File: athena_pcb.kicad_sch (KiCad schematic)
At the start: 8 parts, among them U1 NRF5340-QKAA-R7

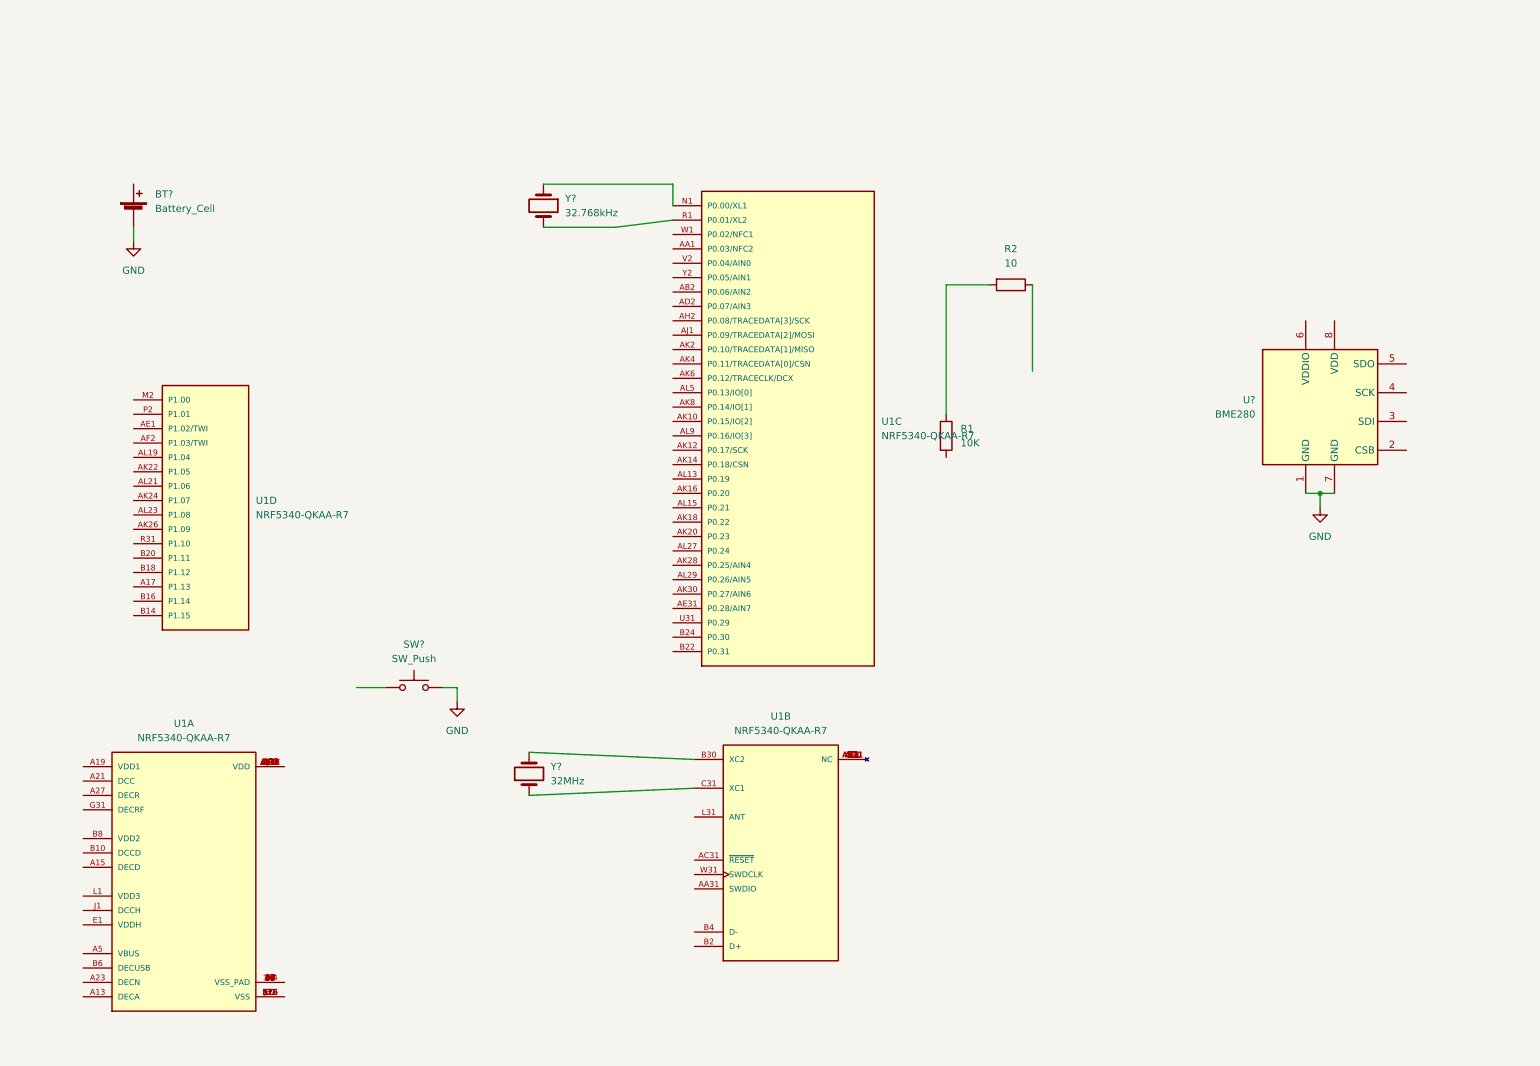
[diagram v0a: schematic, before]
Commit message: Power and Ground connection as per reference schematic
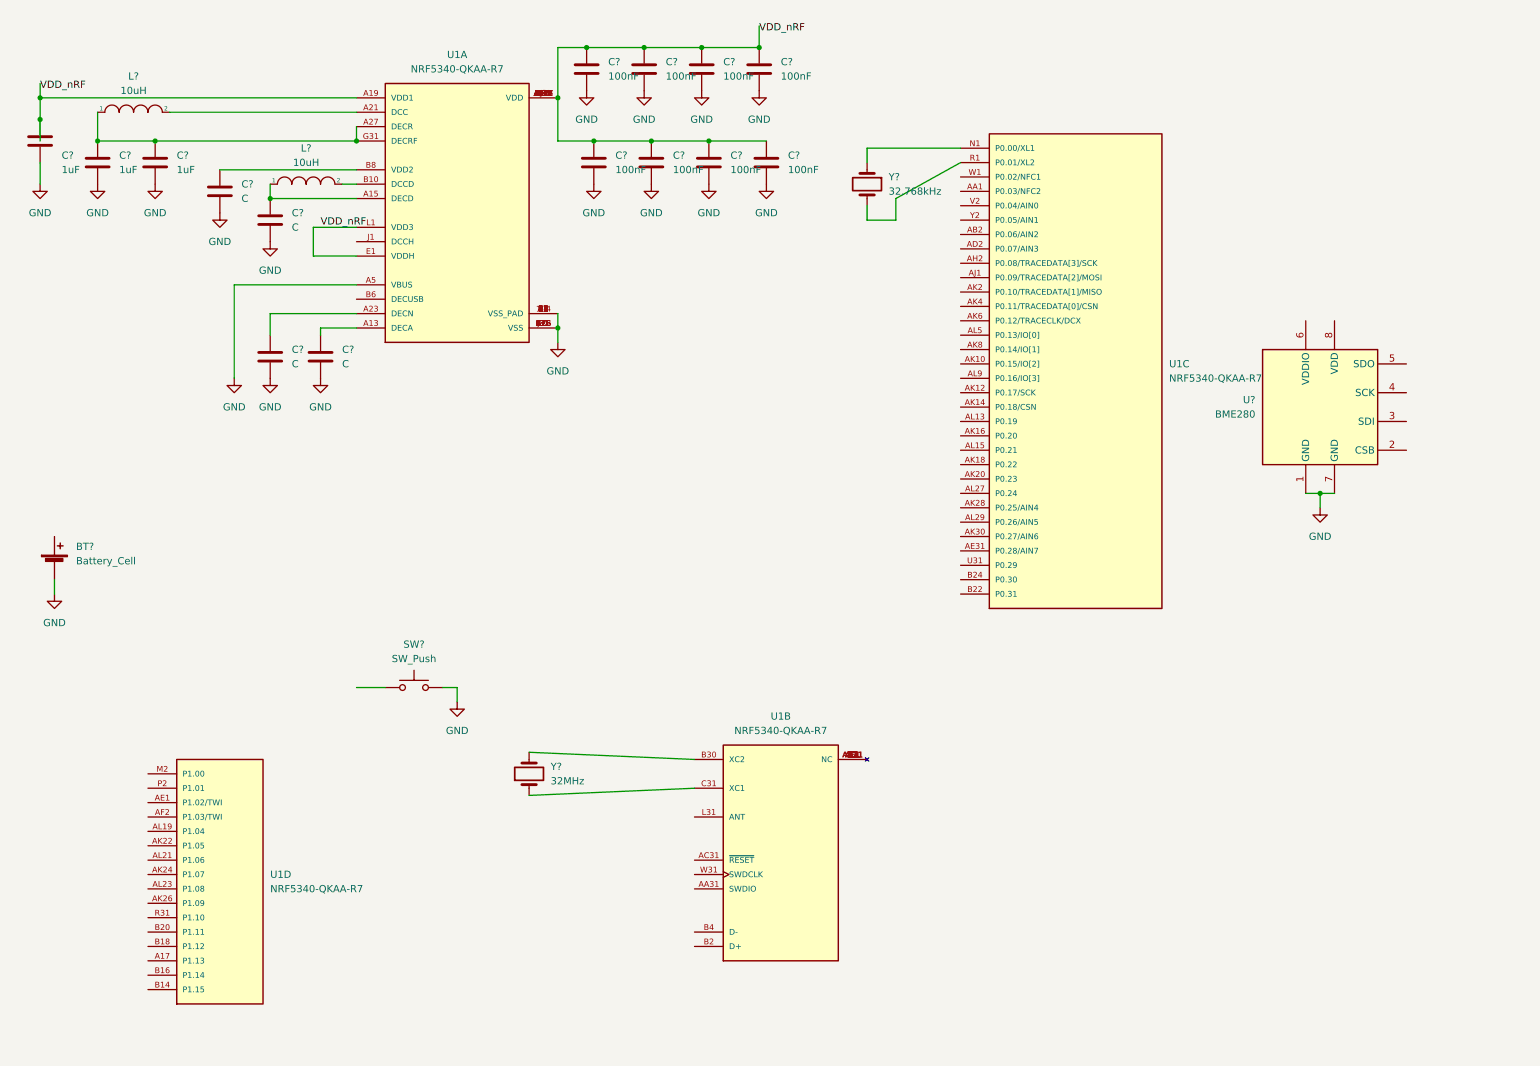
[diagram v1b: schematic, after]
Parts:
- removed R1: 10K, symbol Device:R
- removed R2: 10, symbol Device:R
- added C? (x8): 100nF, symbol Device:C
- added C? (x4): C, symbol Device:C
- added C? (x3): 1uF, symbol Device:C
- added L? (x2): 10uH, symbol pspice:INDUCTOR
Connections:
- net GND: now also U1.104 (VSS_PAD), U1.35 (VSS_PAD), U1.36 (VSS_PAD), U1.37 (VSS_PAD), U1.38 (VSS_PAD), U1.39 (VSS_PAD), U1.40 (VSS_PAD), U1.41 (VSS_PAD), U1.43 (VSS_PAD), U1.44 (VSS_PAD), U1.45 (VSS_PAD), U1.46 (VSS_PAD), U1.47 (VSS_PAD), U1.48 (VSS_PAD), U1.49 (VSS_PAD), U1.50 (VSS_PAD), U1.51 (VSS_PAD), U1.A25 (VSS), U1.A5 (VBUS), U1.B12 (VSS), U1.B26 (VSS), U1.G1 (VSS), U1.H2 (VSS), U1.J31 (VSS), C?.2, C?.2, C?.2, C?.2, C?.2, C?.2, C?.2, C?.2, C?.2, C?.2, C?.2, C?.2, C?.2, C?.2, C?.2
- net at U1.A13 (DECA): now also C?.1
- net at U1.A15 (DECD): now also C?.1, L?.1
- net VDD_nRF: now reaches U1.A19 (VDD1)
- net VDD_nRF: now also U1.AC1 (VDD), U1.AG1 (VDD), U1.AJ31 (VDD), U1.AL11 (VDD), U1.AL17 (VDD), U1.AL25 (VDD), U1.AL3 (VDD), U1.AL7 (VDD), U1.B28 (VDD), U1.C1 (VDD), U1.E1 (VDDH), U1.E31 (VDD), U1.L1 (VDD3), U1.N31 (VDD), U1.U1 (VDD), C?.1, C?.1, C?.1, C?.1, C?.1, C?.1, C?.1, C?.1, C?.1
- net at U1.A21 (DCC): now also L?.2
- net at U1.A23 (DECN): now also C?.1
- net at U1.A27 (DECR): now also U1.G31 (DECRF), C?.1, C?.1, L?.1
- net at U1.B10 (DCCD): now also L?.2
- net at U1.B8 (VDD2): now also C?.1
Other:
- moved on the sheet: BT?, U1A, U1C, U1D, Y?

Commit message: Additional connections made
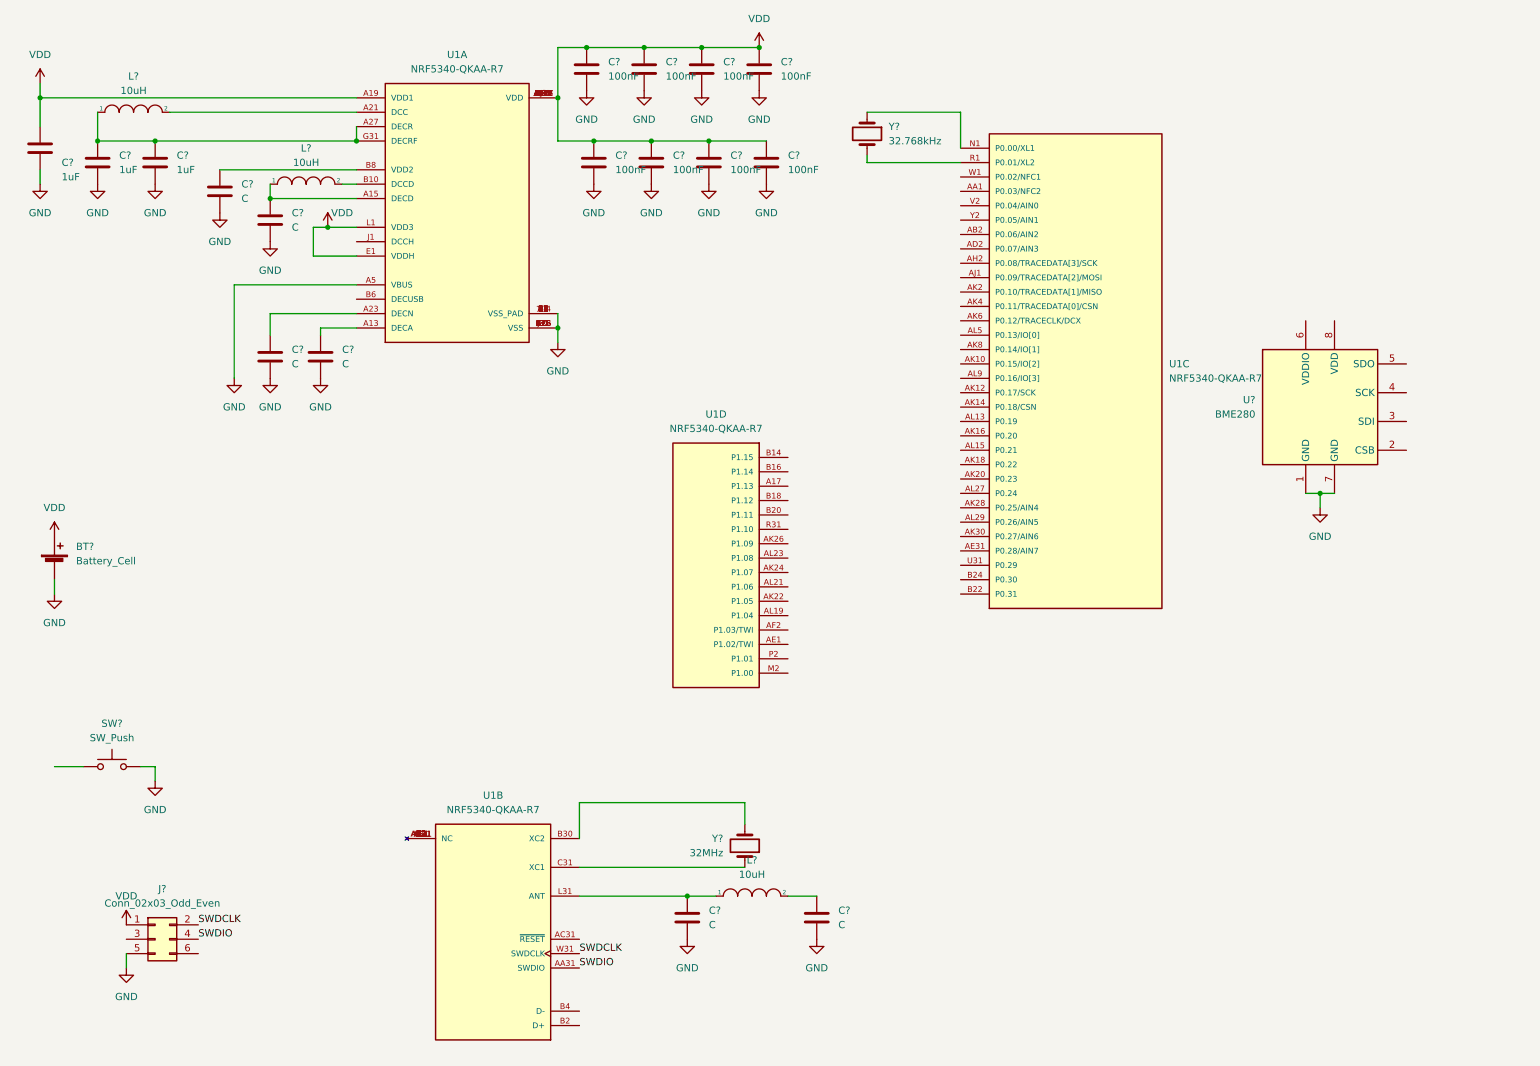
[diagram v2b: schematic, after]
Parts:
- added C? (x2): C, symbol Device:C
- added J?: Conn_02x03_Odd_Even, symbol Connector_Generic:Conn_02x03_Odd_Even
- added L?: 10uH, symbol pspice:INDUCTOR
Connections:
- net VDD_nRF is gone; now on net VDD: C?.1, C?.1, C?.1, C?.1, C?.1, C?.1, C?.1, C?.1, C?.1, U1.A19 (VDD1), U1.AC1 (VDD), U1.AG1 (VDD), U1.AJ31 (VDD), U1.AL11 (VDD), U1.AL17 (VDD), U1.AL25 (VDD), U1.AL3 (VDD), U1.AL7 (VDD), U1.B28 (VDD), U1.C1 (VDD), U1.E1 (VDDH), U1.E31 (VDD), U1.L1 (VDD3), U1.N31 (VDD), U1.U1 (VDD)
- net GND: now also C?.2, C?.2, J?.5 (Pin_5)
- net VDD: now reaches BT?.1 (+)
- net VDD: now also J?.1 (Pin_1)
- net SWDIO: now reaches U1.AA31 (SWDIO)
- net SWDIO: now also J?.4 (Pin_4)
- net at U1.L31 (ANT): now also C?.1, L?.1
- net SWDCLK: now reaches U1.W31 (SWDCLK)
- net SWDCLK: now also J?.2 (Pin_2)
- new net: C?.1, L?.2
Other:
- moved on the sheet: C?, SW?, U1B, U1D, Y?

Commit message: BME280 shcematic done
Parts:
- added C18, C19: 100nF, symbol Device:C
- gave numbers to parts that had none: 26
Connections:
- net GND: now also C18.1, C19.2
- net VDD: now also U2.6 (VDDIO), U2.8 (VDD), C18.2, C19.1
- net CSB: now reaches U2.2 (CSB)
- net SDI_SDA: now reaches U2.3 (SDI)
- net SCK_SCL: now reaches U2.4 (SCK)
- net SDO: now reaches U2.5 (SDO)
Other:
- moved on the sheet: BT1, U1C, U1D, U2, Y2

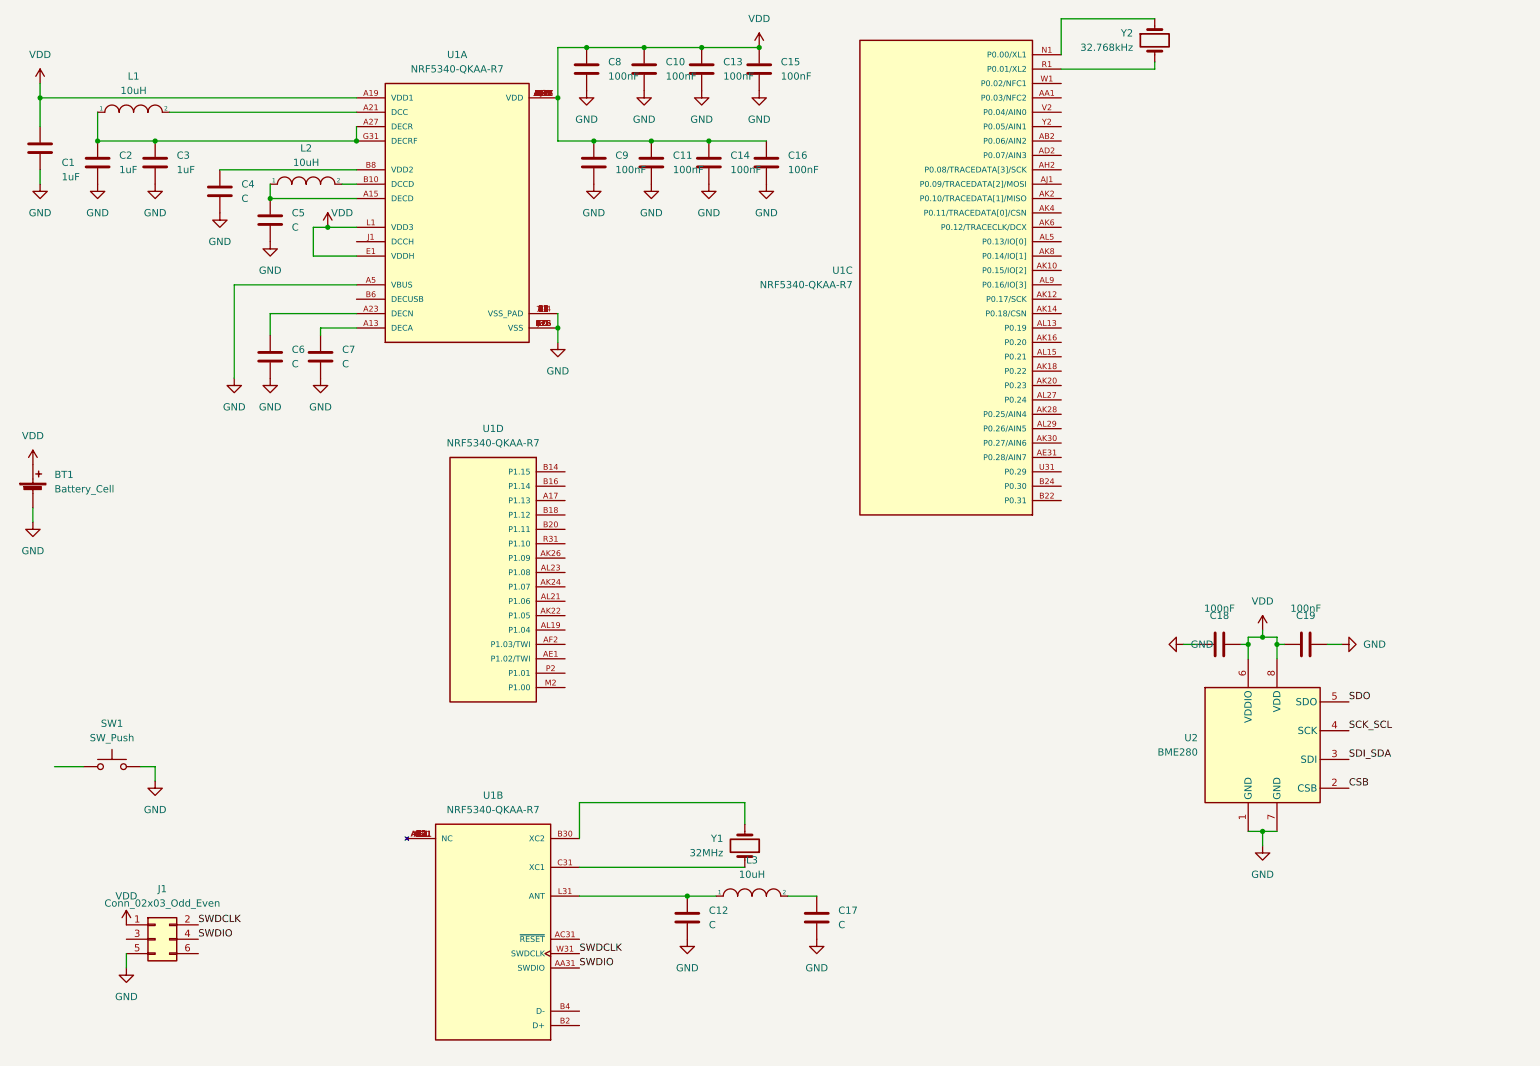
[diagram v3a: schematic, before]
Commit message: Updated to KiCAD 7. Added VBAT Sense
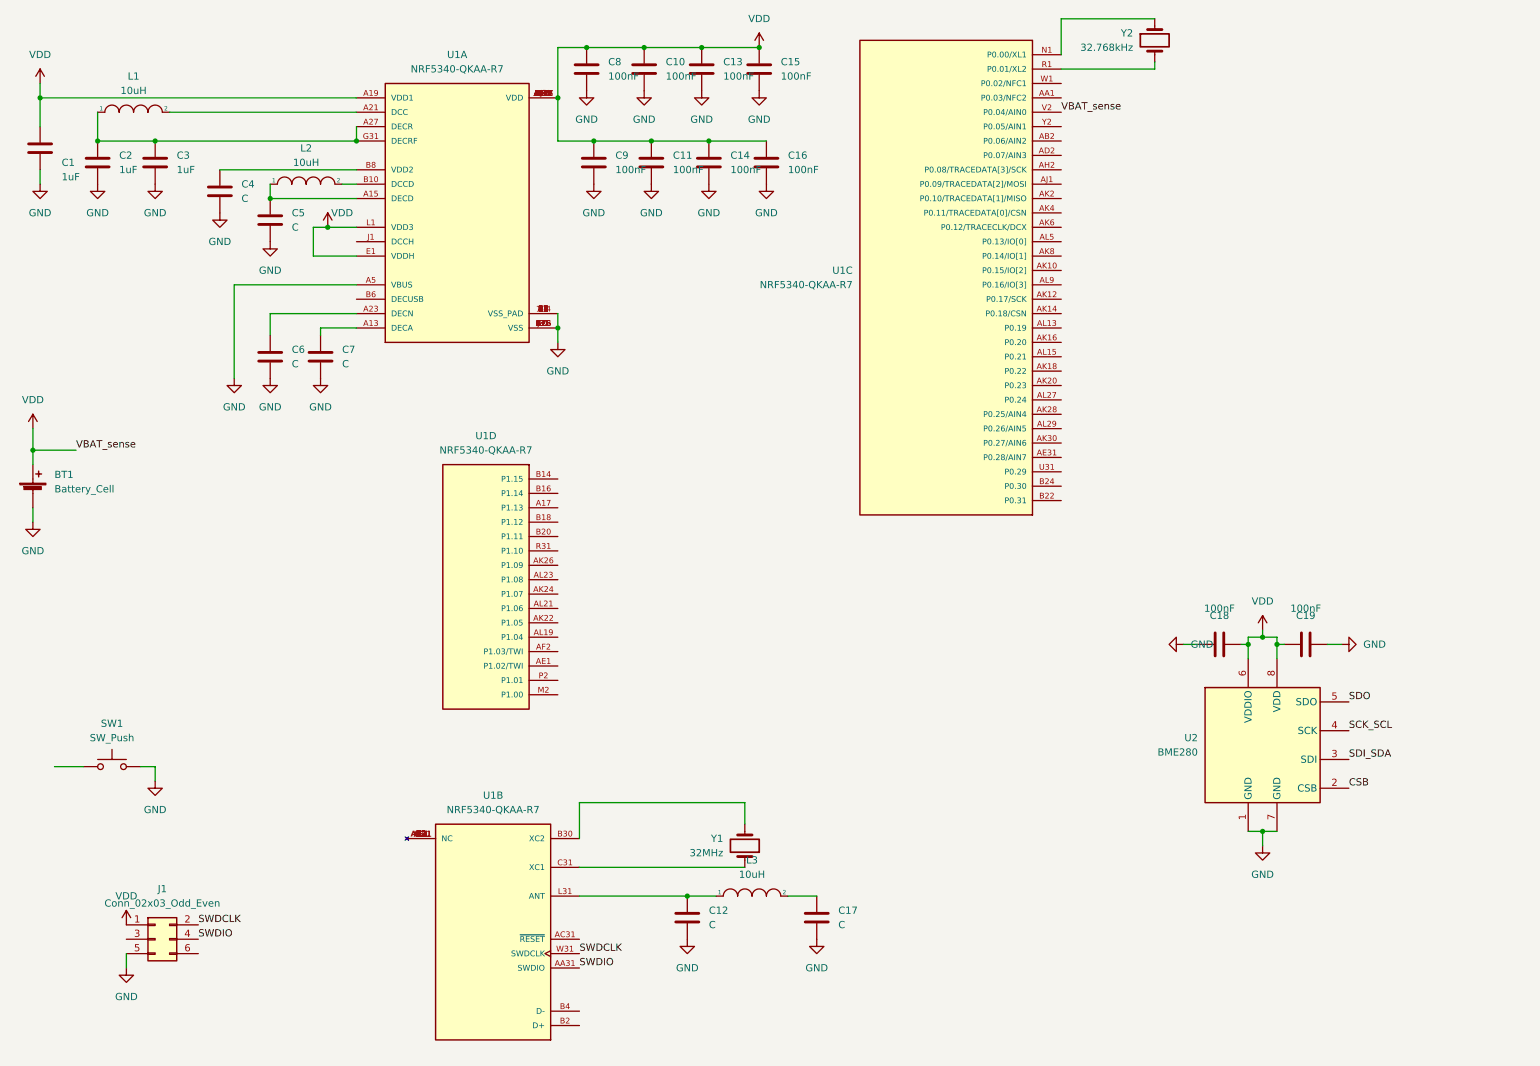
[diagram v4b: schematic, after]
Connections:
- net VDD: now also U1.V2 (P0.04/AIN0)
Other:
- moved on the sheet: U1D
